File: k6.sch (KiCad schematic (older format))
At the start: 20 parts

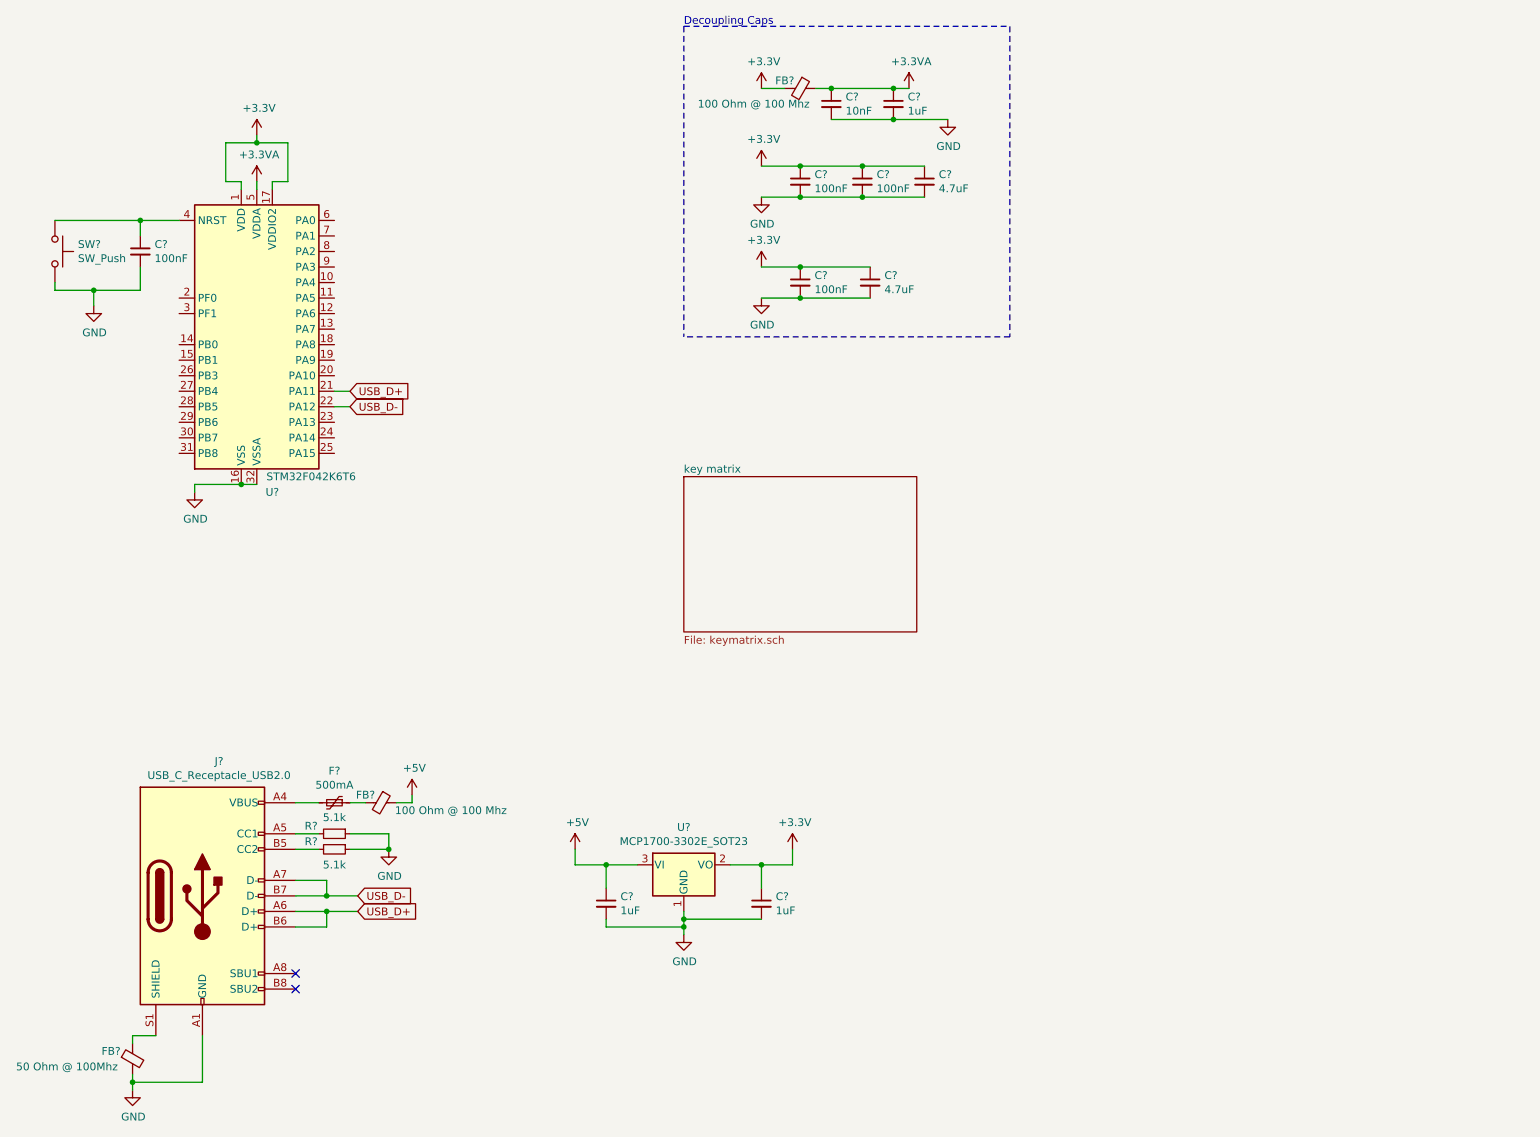
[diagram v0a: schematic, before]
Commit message: Adding SWD pins
Removed the start of the reset circuit and starting to add reset/debugging pins to program pcb (unsure if it will remain in the final but for protos will add).
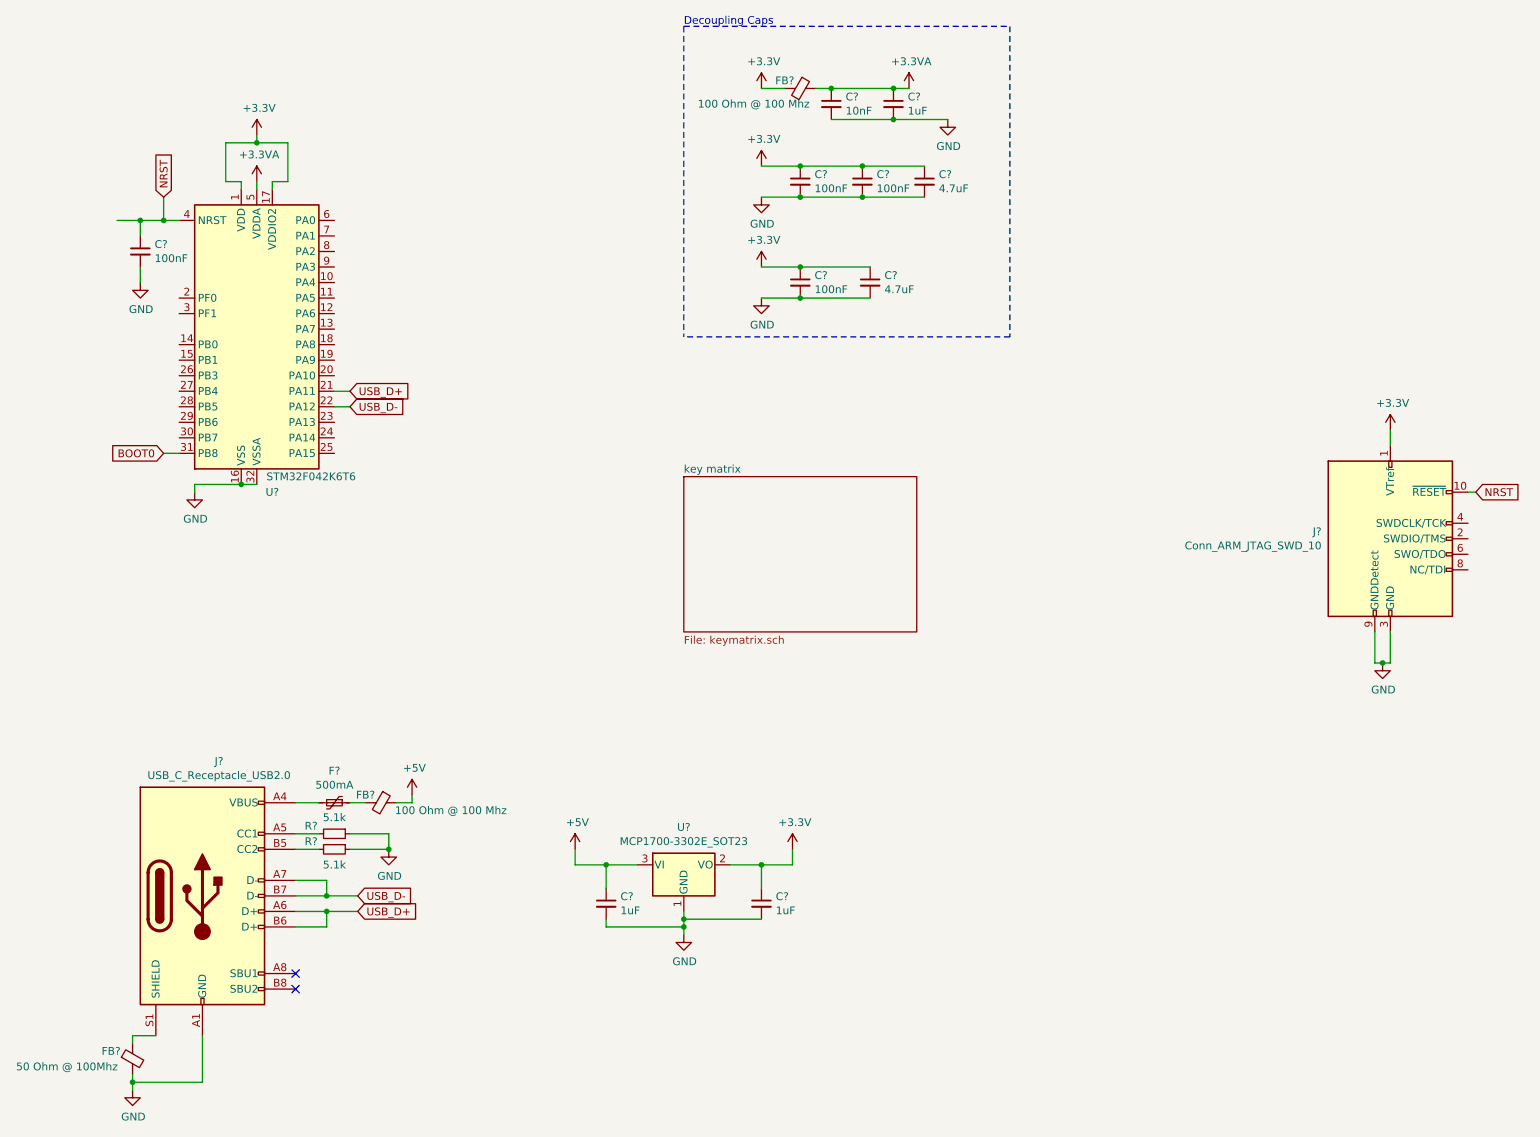
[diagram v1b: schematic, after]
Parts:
- removed SW?: SW_Push, symbol Switch:SW_Push
- added J?: Conn_ARM_JTAG_SWD_10, symbol Connector:Conn_ARM_JTAG_SWD_10
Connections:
- net +3V3: now also J?.1 (VTref)
- net GND: now also J?.3 (GND), J?.5 (GND), J?.9 (GNDDetect)
- net BOOT0: now reaches U?.31 (PB8)
- net NRST: now reaches C?.1, U?.4 (NRST)
- net NRST: now also J?.10 (~RESET~)
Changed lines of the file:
@@
 L power:GND #PWR?
 U 1 1 5EBAB22F
-P 1200 2400
-F 0 "#PWR?" H 1200 2150 50  0001 C CNN
-F 1 "GND" H 1205 2227 50  0000 C CNN
-F 2 "" H 1200 2400 50  0001 C CNN
-F 3 "" H 1200 2400 50  0001 C CNN
-	1    1200 2400
+P 1500 2250
+F 0 "#PWR?" H 1500 2000 50  0001 C CNN
+F 1 "GND" H 1505 2077 50  0000 C CNN
+F 2 "" H 1500 2250 50  0001 C CNN
+F 3 "" H 1500 2250 50  0001 C CNN
+	1    1500 2250
 	1    0    0    -1
 $EndComp
-$Comp
-L Switch:SW_Push SW?
-U 1 1 5EBA659A
-P 950 2050
-F 0 "SW?" V 904 2198 50  0000 L CNN
-F 1 "SW_Push" V 995 2198 50  0000 L CNN
-F 2 "" H 950 2250 50  0001 C CNN
-F 3 "~" H 950 2250 50  0001 C CNN
-	1    950  2050
-	0    1    1    0
-$EndComp
-Wire Wire Line
-	1200 2300 1200 2400
-Wire Wire Line
-	950  2300 950  2250
-Connection ~ 1200 2300
-Wire Wire Line
-	1200 2300 950  2300
 $Comp
 L Device:C_Small C?
@@
 $EndComp
 Wire Wire Line
-	950  1850 1500 1850
-Wire Wire Line
 	1500 1850 1500 1950
-Wire Wire Line
-	1200 2300 1500 2300
-Wire Wire Line
-	1500 2150 1500 2300
 Connection ~ 1500 1850
 Wire Wire Line
-	1500 1850 1750 1850
+	1500 1850 1650 1850
+Wire Wire Line
+	1650 3350 1750 3350
+Text GLabel 1650 3350 0    50   Input ~ 0
+BOOT0
+Wire Wire Line
+	1350 1850 1500 1850
+Wire Wire Line
+	1500 2250 1500 2150
+$Comp
+L Connector:Conn_ARM_JTAG_SWD_10 J?
+U 1 1 5EC9B818
+P 9550 3900
+F 0 "J?" H 9107 3946 50  0000 R CNN
+F 1 "Conn_ARM_JTAG_SWD_10" H 9107 3855 50  0000 R CNN
+F 2 "" H 9550 3900 50  0001 C CNN
+F 3 "http://infocenter.arm.com/help/topic/com.arm.doc.ddi0314h/DDI0314H_coresight_components_trm.pdf" V 9200 2650 50  0001 C CNN
+	1    9550 3900
+	1    0    0    -1
+$EndComp
+$Comp
+L power:+3.3V #PWR?
+U 1 1 5EC9F1EB
+P 9550 3200
+F 0 "#PWR?" H 9550 3050 50  0001 C CNN
+F 1 "+3.3V" H 9565 3373 50  0000 C CNN
+F 2 "" H 9550 3200 50  0001 C CNN
+F 3 "" H 9550 3200 50  0001 C CNN
+	1    9550 3200
+	1    0    0    -1
+$EndComp
+Wire Wire Line
+	9550 3200 9550 3300
+$Comp
+L power:GND #PWR?
+U 1 1 5ECA1ECD
+P 9500 4700
+F 0 "#PWR?" H 9500 4450 50  0001 C CNN
+F 1 "GND" H 9505 4527 50  0000 C CNN
+F 2 "" H 9500 4700 50  0001 C CNN
+F 3 "" H 9500 4700 50  0001 C CNN
+	1    9500 4700
+	1    0    0    -1
+$EndComp
+Wire Wire Line
+	9500 4700 9450 4700
+Wire Wire Line
+	9450 4700 9450 4500
+Wire Wire Line
+	9550 4500 9550 4700
+Wire Wire Line
+	9550 4700 9500 4700
+Connection ~ 9500 4700
+Text GLabel 10100 3600 2    50   Input ~ 0
+NRST
+Wire Wire Line
+	10100 3600 10050 3600
+Text GLabel 1650 1700 1    50   Input ~ 0
+NRST
+Wire Wire Line
+	1650 1700 1650 1850
+Connection ~ 1650 1850
+Wire Wire Line
+	1650 1850 1750 1850
 $EndSCHEMATC

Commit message: Start PCB Design
Get barebones parts selected
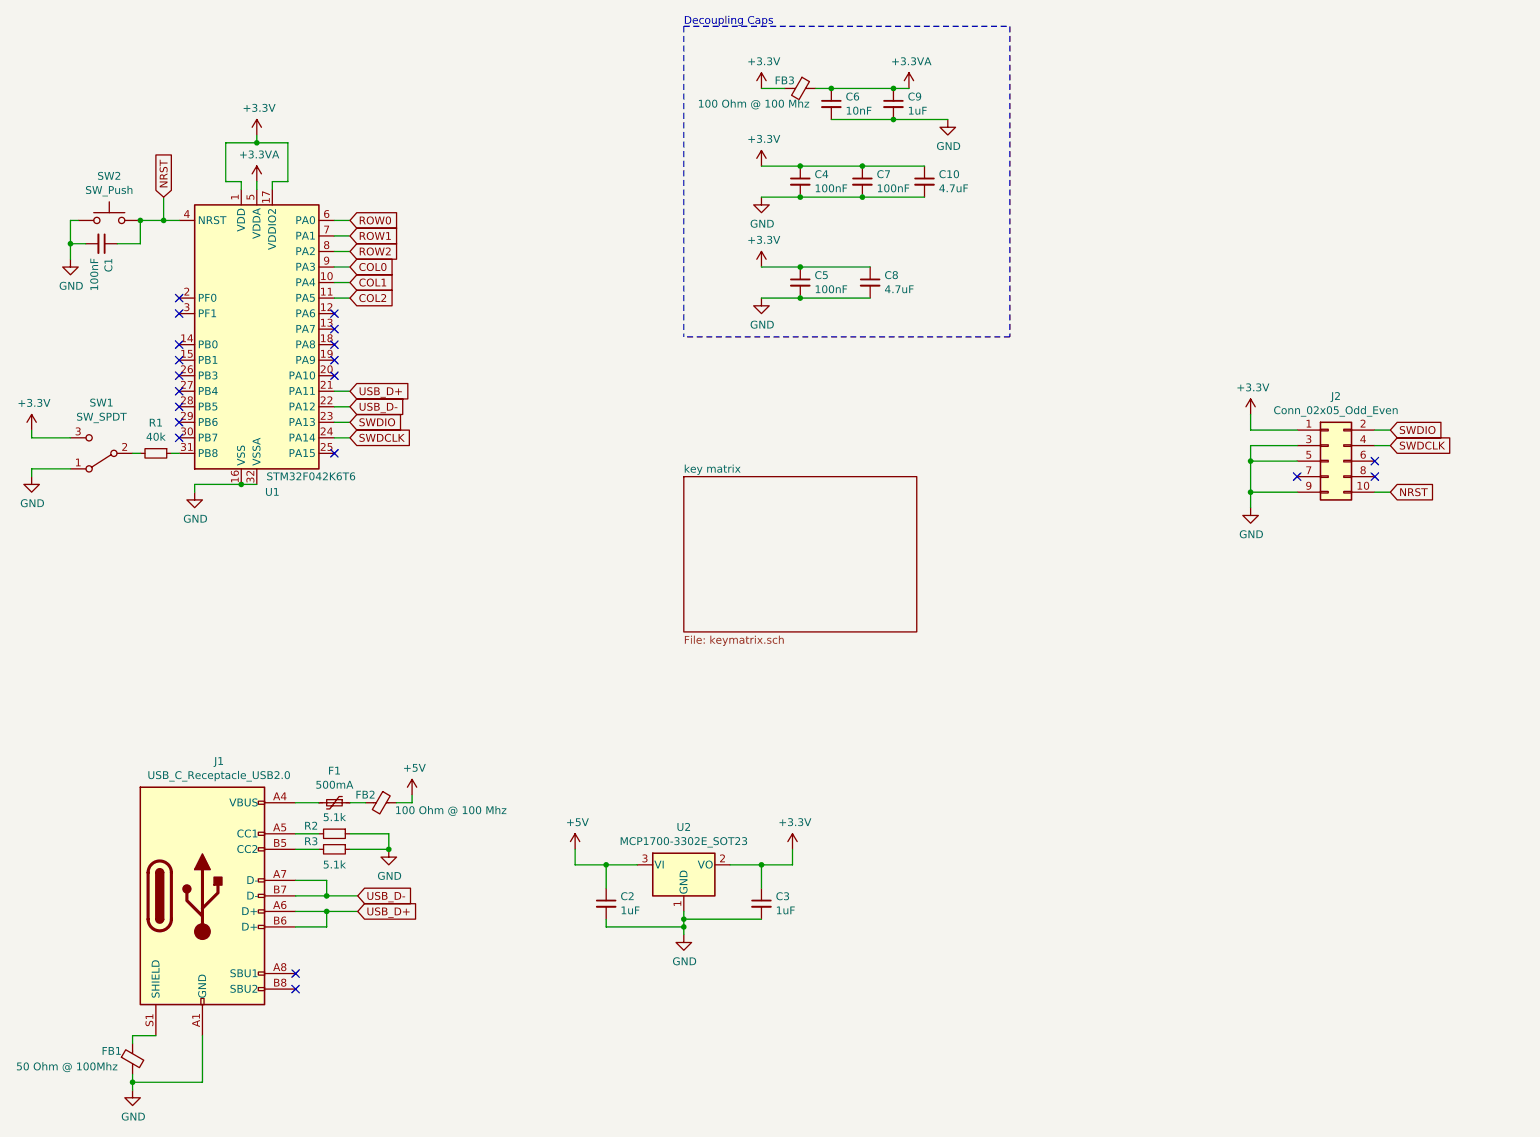
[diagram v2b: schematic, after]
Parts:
- removed J?: Conn_ARM_JTAG_SWD_10, symbol Connector:Conn_ARM_JTAG_SWD_10
- added J2: Conn_02x05_Odd_Even, Connector_PinHeader_2.00mm:PinHeader_2x05_P2.00mm_Vertical, symbol Connector_Generic:Conn_02x05_Odd_Even
- added R1: 40k, Resistor_SMD:R_0805_2012Metric_Pad1.15x1.40mm_HandSolder, symbol Device:R_Small
- added SW1: SW_SPDT, Button_Switch_SMD:SW_SPDT_CK-JS102011SAQN, symbol Switch:SW_SPDT
- added SW2: SW_Push, Button_Switch_SMD:SW_SPST_B3U-1000P, symbol Switch:SW_Push
- C1, C10, C2, C3, C4, C5, C6, C7, C8, C9: renamed from C?; footprint (none) -> Capacitor_SMD:C_0805_2012Metric_Pad1.15x1.40mm_HandSolder
- F1: renamed from F?; footprint (none) -> Fuse:Fuse_1206_3216Metric
- FB1, FB2, FB3: renamed from FB?; footprint (none) -> Inductor_SMD:L_0603_1608Metric_Pad1.05x0.95mm_HandSolder
- J1: renamed from J?; footprint (none) -> Connector_USB:USB_C_Receptacle_HRO_TYPE-C-31-M-12
- R2, R3: renamed from R?; footprint (none) -> Resistor_SMD:R_0805_2012Metric_Pad1.15x1.40mm_HandSolder
- gave numbers to parts that had none: 2
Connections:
- net +3V3: now also J2.1 (Pin_1), SW1.3 (C)
- net GND: now also J2.3 (Pin_3), J2.5 (Pin_5), J2.9 (Pin_9), SW1.1 (A), SW2.1
- net NRST: now also J2.10 (Pin_10), SW2.2
- net COL1: now reaches U1.10 (PA4)
- net COL2: now reaches U1.11 (PA5)
- net SWDIO: now reaches U1.23 (PA13)
- net SWDIO: now also J2.2 (Pin_2)
- net SWDCLK: now reaches U1.24 (PA14)
- net SWDCLK: now also J2.4 (Pin_4)
- net ROW0: now reaches U1.6 (PA0)
- net ROW1: now reaches U1.7 (PA1)
- net ROW2: now reaches U1.8 (PA2)
- net COL0: now reaches U1.9 (PA3)
- net BOOT0: no longer names the net of U1.31 (PB8)
- net BOOT0: now also R1.1
- new net: R1.2, SW1.2 (B)
- no-connect marks 2 -> 20
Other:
- moved on the sheet: C1

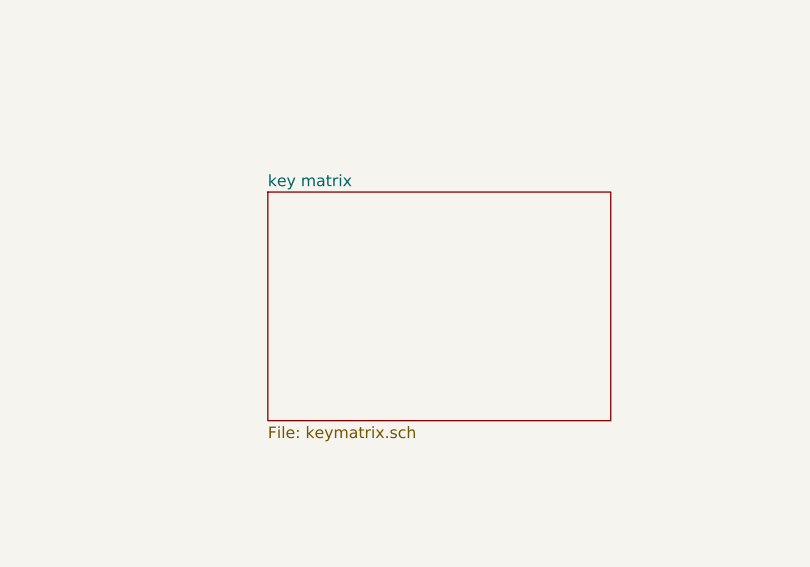
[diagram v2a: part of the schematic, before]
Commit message: Move parts - part one
No traces yet, only part movement
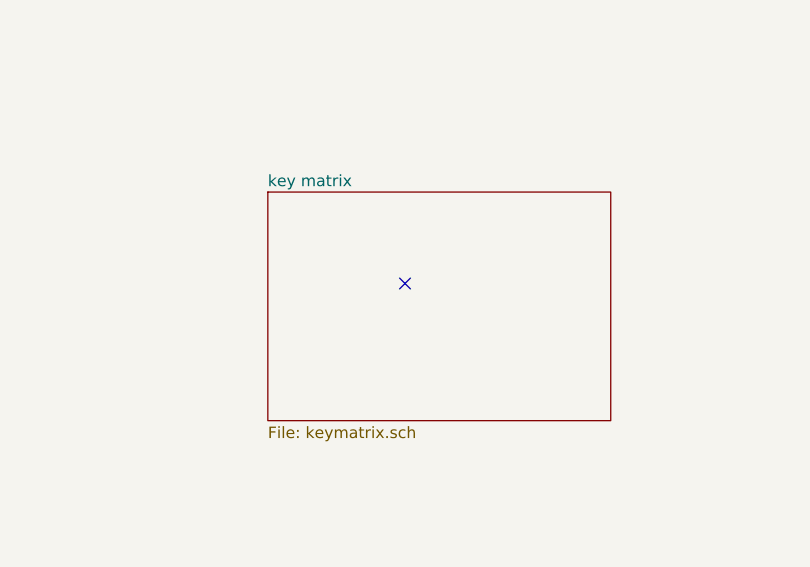
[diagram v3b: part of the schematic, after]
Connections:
- no-connect marks 20 -> 21
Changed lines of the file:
@@
 	1    0    0    -1
 $EndComp
+NoConn ~ 5600 3900
 $EndSCHEMATC

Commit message: Add some tracks - hate it
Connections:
- net ROW0: now also U1.12 (PA6); no longer U1.6 (PA0)
- net ROW1: now also U1.13 (PA7); no longer U1.7 (PA1)
- net ROW2: now also U1.18 (PA8); no longer U1.8 (PA2)
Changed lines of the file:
@@
 $EndDescr
-$Comp
-L MCU_ST_STM32F0:STM32F042K6Tx U1
-U 1 1 5EB61287
-P 2250 2550
-F 0 "U1" H 2350 1500 50  0000 C CNN
-F 1 "STM32F042K6T6" H 2600 1600 50  0000 C CNN
-F 2 "Package_QFP:LQFP-32_7x7mm_P0.8mm" H 1850 1650 50  0001 R CNN
-F 3 "http://www.st.com/st-web-ui/static/active/en/resource/technical/document/datasheet/DM00105814.pdf" H 2250 2550 50  0001 C CNN
-	1    2250 2550
-	1    0    0    -1
-$EndComp
 $Comp
 L Connector:USB_C_Receptacle_USB2.0 J1
@@
 $EndSheet
 Wire Wire Line
-	2150 3550 2250 3550
-Wire Wire Line
 	1850 3600 1850 3550
-Connection ~ 2150 3550
-Wire Wire Line
-	1850 3550 2150 3550
 $Comp
 L power:GND #PWR05
@@
 Wire Wire Line
 	1100 1850 1050 1850
-Text GLabel 2850 1850 2    50   Input ~ 0
+Text GLabel 2850 2450 2    50   Input ~ 0
 ROW0
-Text GLabel 2850 1950 2    50   Input ~ 0
+Text GLabel 2850 2550 2    50   Input ~ 0
 ROW1
-Text GLabel 2850 2050 2    50   Input ~ 0
+Text GLabel 2850 2650 2    50   Input ~ 0
 ROW2
 Text GLabel 2850 2150 2    50   Input ~ 0
@@
 COL2
 Wire Wire Line
-	2750 1850 2850 1850
-Wire Wire Line
-	2850 1950 2750 1950
-Wire Wire Line
-	2750 2050 2850 2050
-Wire Wire Line
 	2850 2150 2750 2150
 Wire Wire Line
@@
 Wire Wire Line
 	2850 2350 2750 2350
-NoConn ~ 2750 2450
-NoConn ~ 2750 2550
-NoConn ~ 2750 2650
 NoConn ~ 2750 2750
 NoConn ~ 2750 2850
@@
 $EndComp
 NoConn ~ 5600 3900
+Connection ~ 2150 3550
+Wire Wire Line
+	1850 3550 2150 3550
+Wire Wire Line
+	2150 3550 2250 3550
+$Comp
+L MCU_ST_STM32F0:STM32F042K6Tx U1
+U 1 1 5EB61287
+P 2250 2550
+F 0 "U1" H 2350 1500 50  0000 C CNN
+F 1 "STM32F042K6T6" H 2600 1600 50  0000 C CNN
+F 2 "Package_QFP:LQFP-32_7x7mm_P0.8mm" H 1850 1650 50  0001 R CNN
+F 3 "http://www.st.com/st-web-ui/static/active/en/resource/technical/document/datasheet/DM00105814.pdf" H 2250 2550 50  0001 C CNN
+	1    2250 2550
+	1    0    0    -1
+$EndComp
+Wire Wire Line
+	2750 2650 2850 2650
+Wire Wire Line
+	2850 2550 2750 2550
+Wire Wire Line
+	2750 2450 2850 2450
+NoConn ~ 2750 1850
+NoConn ~ 2750 1950
+NoConn ~ 2750 2050
 $EndSCHEMATC
